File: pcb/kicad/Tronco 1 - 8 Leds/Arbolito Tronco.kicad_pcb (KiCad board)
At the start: 2 copper layers, 68.2 x 100.6 mm, 31 parts, among them U1 WS2812B, U2 WS2812B, U3 WS2812B, U4 WS2812B, U5 WS2812B, U6 WS2812B, U7 WS2812B, U8 WS2812B

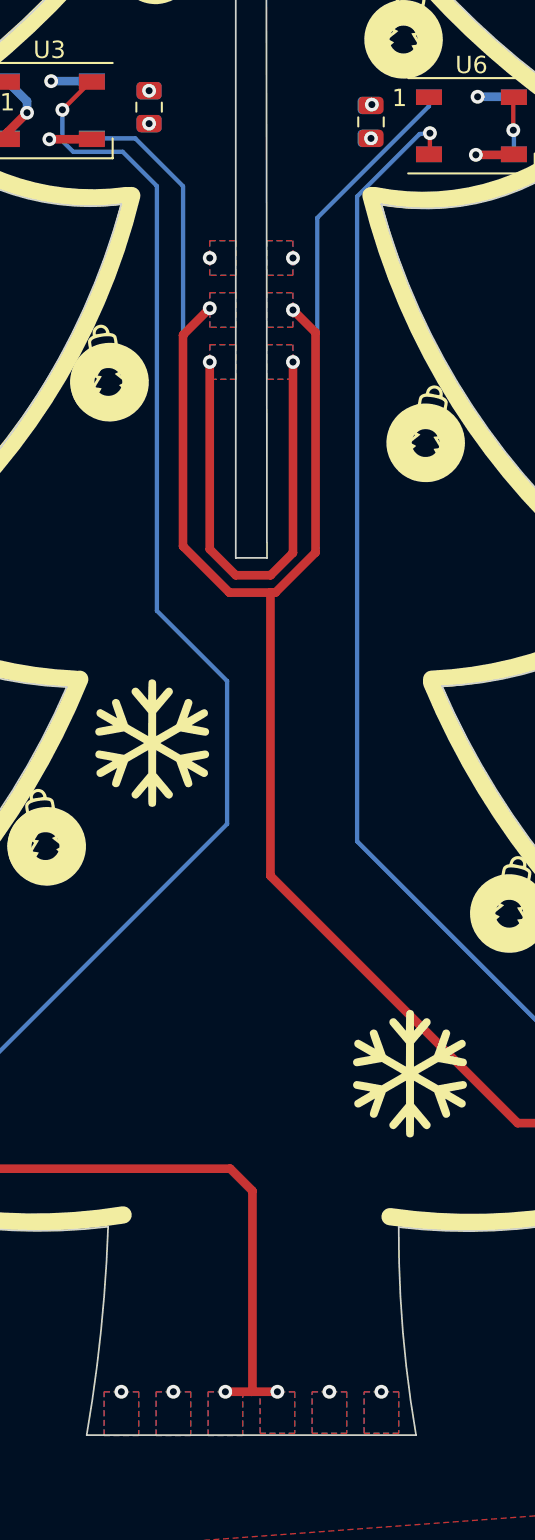
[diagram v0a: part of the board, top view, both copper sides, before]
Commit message: Footprints corrected
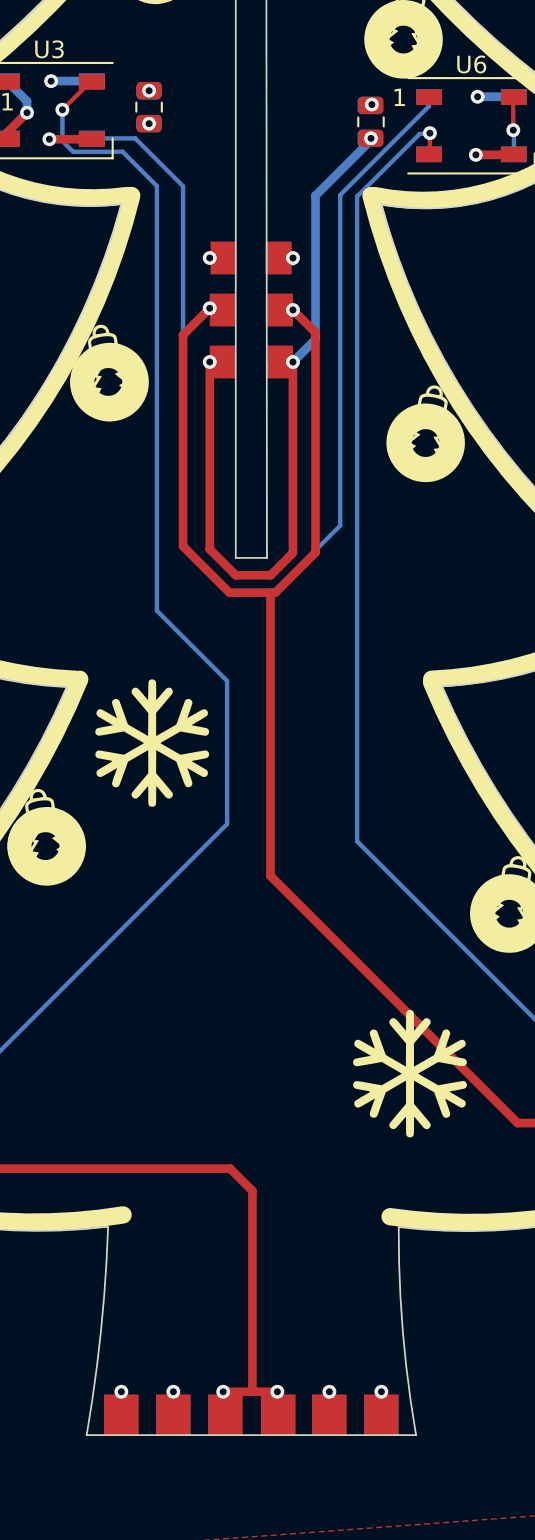
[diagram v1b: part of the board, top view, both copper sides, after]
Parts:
- added J1: Conn_01x01, Library:Input, F.Cu at (138.0, 128.8)
- added J10: Conn_01x01, Library:Output, F.Cu at (141.1, 62.1)
- added J11: Conn_01x01, Library:Output, F.Cu at (137.8, 68.1)
- added J12: Conn_01x01, Library:Output, F.Cu at (141.2, 68.1)
- added J2: Conn_01x01, Library:Input, F.Cu at (141.1, 128.8)
- added J3: Conn_01x01, Library:Input, F.Cu at (132.0, 128.8)
- added J4: Conn_01x01, Library:Input, F.Cu at (135.0, 128.8)
- added J5: Conn_01x01, Library:Input, F.Cu at (144.0, 128.8)
- added J6: Conn_01x01, Library:Input, F.Cu at (147.0, 128.8)
- added J7: Conn_01x01, Library:Output, F.Cu at (141.2, 65.1)
- added J8: Conn_01x01, Library:Output, F.Cu at (137.8, 65.1)
- added J9: Conn_01x01, Library:Output, F.Cu at (137.9, 62.1)
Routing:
- net GND: track 40.0 -> 54.8 mm
- removed copper zone on B.Cu, net +5V
- removed copper zone on B.Cu, net /DIN
- removed copper zone on F.Cu, net /DIN
- removed copper zone on B.Cu, net /Dout
- removed copper zone on F.Cu, net /Dout
- removed copper zone on F.Cu, net GND

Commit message: Pre USB change
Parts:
- U1, U2, U3, U4, U5, U6, U7, U8: footprint LED_SMD:LED_WS2812B_PLCC4_5.0x5.0mm_P3.2mm -> Library:LED_WS2812B_PLCC4_5.0x5.0mm_P3.2mm

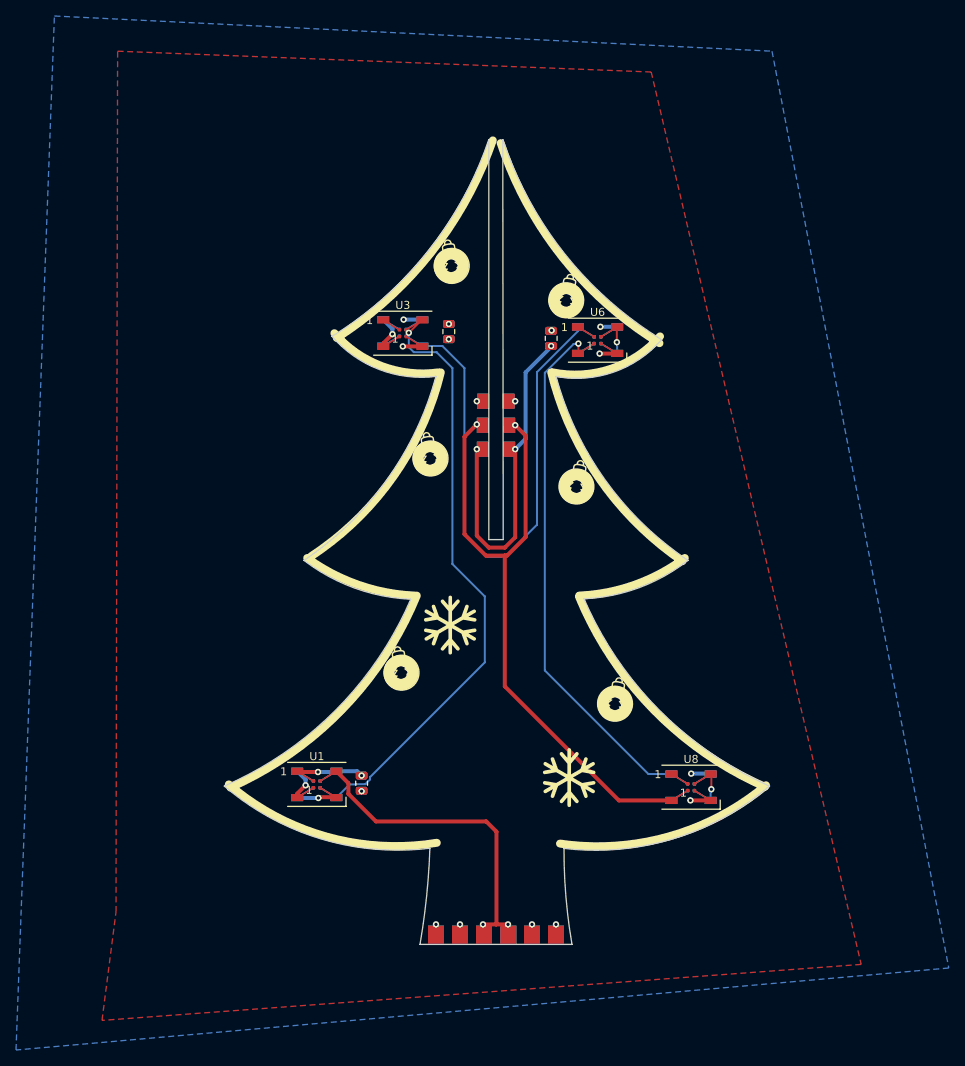
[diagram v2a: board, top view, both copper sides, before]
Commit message: Led Footprint Changed
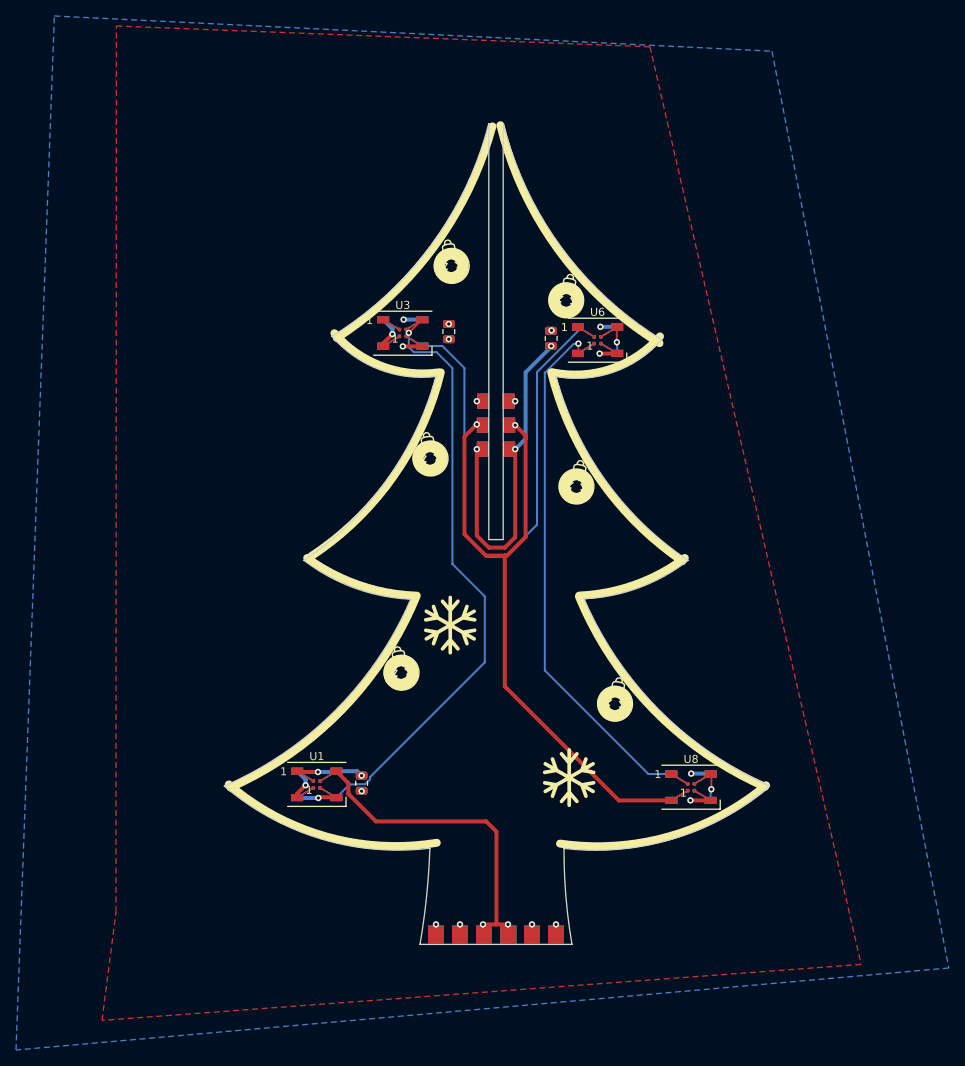
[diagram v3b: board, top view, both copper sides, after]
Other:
- board size 68.2 x 100.6 mm -> 68.2 x 102.6 mm
